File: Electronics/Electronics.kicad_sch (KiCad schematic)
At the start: 0 parts

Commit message: started esp32
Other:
- added sheet Telemetry Module (Telemetry_Module.kicad_sch)
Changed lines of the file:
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@@
 (kicad_sch (version 20230121) (generator eeschema)
   (paper "A4")
+  (sheet (at 132.08 72.39) (size 19.05 19.05) (fields_autoplaced)
+    (stroke (width 0.1524) (type solid))
+    (fill (color 0 0 0 0.0000))
+    (property "Sheetname" "Telemetry Module" (at 132.08 71.6784 0)
+      (effects (font (size 1.27 1.27)) (justify left bottom))
+    )
+    (property "Sheetfile" "Telemetry_Module.kicad_sch" (at 132.08 92.0246 0)
+      (effects (font (size 1.27 1.27)) (justify left top))
+    )
+    (instances
+      (project "Electronics"
+        (path "/4c70cac4-2e87-4919-a1c8-fe5f41acf493" (page "3"))
+      )
+    )
+  )
   (sheet (at 76.2 71.12) (size 21.59 24.13) (fields_autoplaced)
     (stroke (width 0.1524) (type solid))

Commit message: BMI270 schem
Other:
- added sheet Gyroscope (bmi270.kicad_sch)
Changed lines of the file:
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@@
+    )
+  )
+  (sheet (at 138.43 107.95) (size 21.59 20.32) (fields_autoplaced)
+    (stroke (width 0.1524) (type solid))
+    (fill (color 0 0 0 0.0000))
+    (property "Sheetname" "Gyroscope" (at 138.43 107.2384 0)
+      (effects (font (size 1.27 1.27)) (justify left bottom))
+    )
+    (property "Sheetfile" "bmi270.kicad_sch" (at 138.43 128.8546 0)
+      (effects (font (size 1.27 1.27)) (justify left top))
+    )
+    (instances
+      (project "Electronics"
+        (path "/4c70cac4-2e87-4919-a1c8-fe5f41acf493" (page "4"))
+      )
     )
   )

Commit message: rename telemetry
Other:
- sheet Gyroscope renamed Gyro Controller
- sheet Telemetry Module renamed Telemetry and Control Module
- sheet Gyro Controller: file bmi270.kicad_sch -> Gyro_Controller.kicad_sch
- sheet Telemetry and Control Module: file Telemetry_Module.kicad_sch -> Telemetry_And_Control.kicad_sch
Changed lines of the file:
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@@
     (stroke (width 0.1524) (type solid))
     (fill (color 0 0 0 0.0000))
-    (property "Sheetname" "Telemetry Module" (at 132.08 71.6784 0)
+    (property "Sheetname" "Telemetry and Control Module" (at 132.08 71.6784 0)
       (effects (font (size 1.27 1.27)) (justify left bottom))
     )
-    (property "Sheetfile" "Telemetry_Module.kicad_sch" (at 132.08 92.0246 0)
+    (property "Sheetfile" "Telemetry_And_Control.kicad_sch" (at 132.08 92.0246 0)
       (effects (font (size 1.27 1.27)) (justify left top))
     )
@@
     )
   )
-  (sheet (at 138.43 107.95) (size 21.59 20.32) (fields_autoplaced)
+  (sheet (at 76.2 104.14) (size 21.59 20.32) (fields_autoplaced)
     (stroke (width 0.1524) (type solid))
     (fill (color 0 0 0 0.0000))
-    (property "Sheetname" "Gyroscope" (at 138.43 107.2384 0)
+    (property "Sheetname" "Gyro Controller" (at 76.2 103.4284 0)
       (effects (font (size 1.27 1.27)) (justify left bottom))
     )
-    (property "Sheetfile" "bmi270.kicad_sch" (at 138.43 128.8546 0)
+    (property "Sheetfile" "Gyro_Controller.kicad_sch" (at 76.2 125.0446 0)
       (effects (font (size 1.27 1.27)) (justify left top))
     )

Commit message: updates
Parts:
- added BT1: Battery, symbol Device:Battery
- added BT2: 4xAA, symbol Device:Battery
- added C29, C44: 22uF, symbol Device:C_Polarized
- added C43: C, symbol Device:C
- added D6: D, symbol Device:D
- added P1: USB_C_Plug_USB2.0, symbol Connector:USB_C_Plug_USB2.0
- added R18, R19, R21: 1k, symbol Device:R
- added SW5: SW_DIP_x02, symbol Switch:SW_DIP_x02
- added U10: ~, Package_DFN_QFN:QFN-16-1EP_3x3mm_P0.5mm_EP1.7x1.7mm, symbol FSUSB74:FSUSB74
- added U11, U12: AMS1117-3.3, Package_TO_SOT_SMD:SOT-223-3_TabPin2, symbol Regulator_Linear:AMS1117-3.3
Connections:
- new net: BT1.2 (-), U12.1 (GND)
- new net: BT2.1 (+), U12.3 (VI)
- new net: R19.1, SW5.3, U10.6 (SEL0)
- new net: R21.1, U10.15 (/OE)
- new net: R18.1, SW5.4, U10.5 (SEL1)
- new net: D6.1 (K), P1.A4 (VBUS), P1.A9 (VBUS), P1.B4 (VBUS), P1.B9 (VBUS), U11.3 (VI)
- new net: BT1.1 (+), BT2.2 (-)
- new net D+: P1.A6 (D+), U10.2 (D+)
- new net D-: P1.A7 (D-), U10.3 (D-)
- new net GND: C29.2, P1.A1 (GND), P1.A12 (GND), P1.B1 (GND), P1.B12 (GND), P1.S1 (SHIELD), R18.2, R19.2, R21.2, U10.1 (GND), U11.1 (GND)
- new net Gyro Controller/USB+: U10.13 (HSD0+)
- new net Gyro Controller/USB-: U10.14 (HSD0-)
- new net Motor Controller/USB+: U10.11 (HSD1+)
- new net Motor Controller/USB-: U10.12 (HSD1-)
- new net VCC: C29.1, D6.2 (A), SW5.1, SW5.2, U10.4 (VCC), U11.2 (VO)
- no-connect marks 0 -> 4
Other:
- sheet Gyro Controller ports: added READY, SCL, SDA, USB+, USB-; removed none
- sheet Motor Controller ports: added ML_A1, ML_A2, ML_B1, ML_B2, MR_A1, MR_A2, MR_B1, MR_B2, READY, SCL, SDA, USB+, USB-, VBAT; removed none

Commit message: mostly done, needs review, needs pins
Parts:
- added R25, R26: 2.2k, symbol Device:R
- C43: value C -> 100nF
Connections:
- net Gyro Controller/SCL: now also R26.2
- net Gyro Controller/SDA: now also R25.2
- net VCC: now also C43.1, C44.1, U12.2 (VO), R25.1, R26.1
- net at C44.2: now also BT1.2 (-), C43.2, U12.1 (GND)
- net VBAT: now reaches BT2.1 (+), U12.3 (VI)
- net Telemetry and Control Module/USB+: now reaches U10.10 (HSD2+)
- net Telemetry and Control Module/USB-: now reaches U10.9 (HSD2-)
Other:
- sheet Telemetry and Control Module ports: added SCL, SDA, USB+, USB-; removed none
- moved on the sheet: BT1, BT2, C29, C43, C44, D6, P1, R18, R19, R21, SW5, U10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

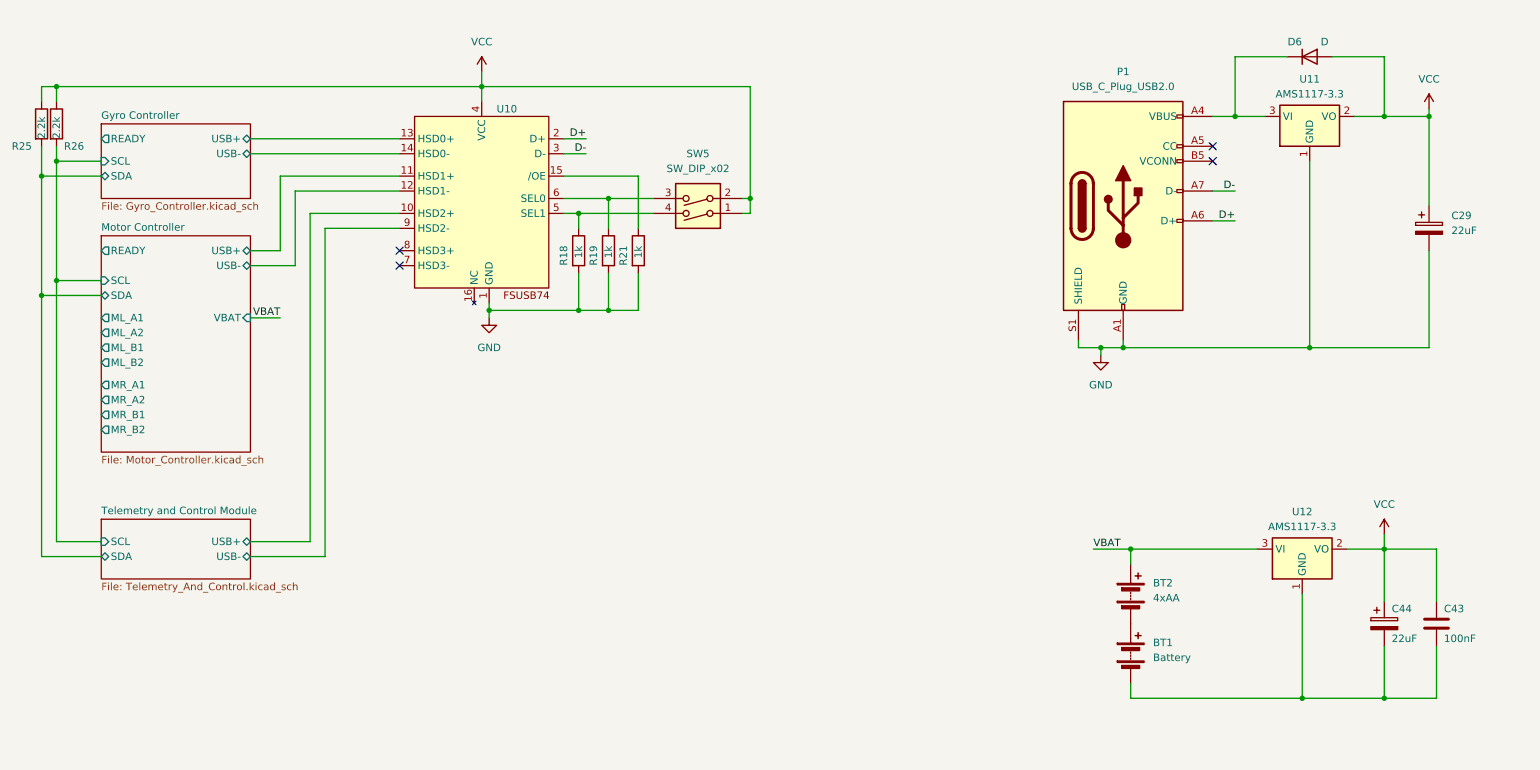
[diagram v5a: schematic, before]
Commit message: oled displays
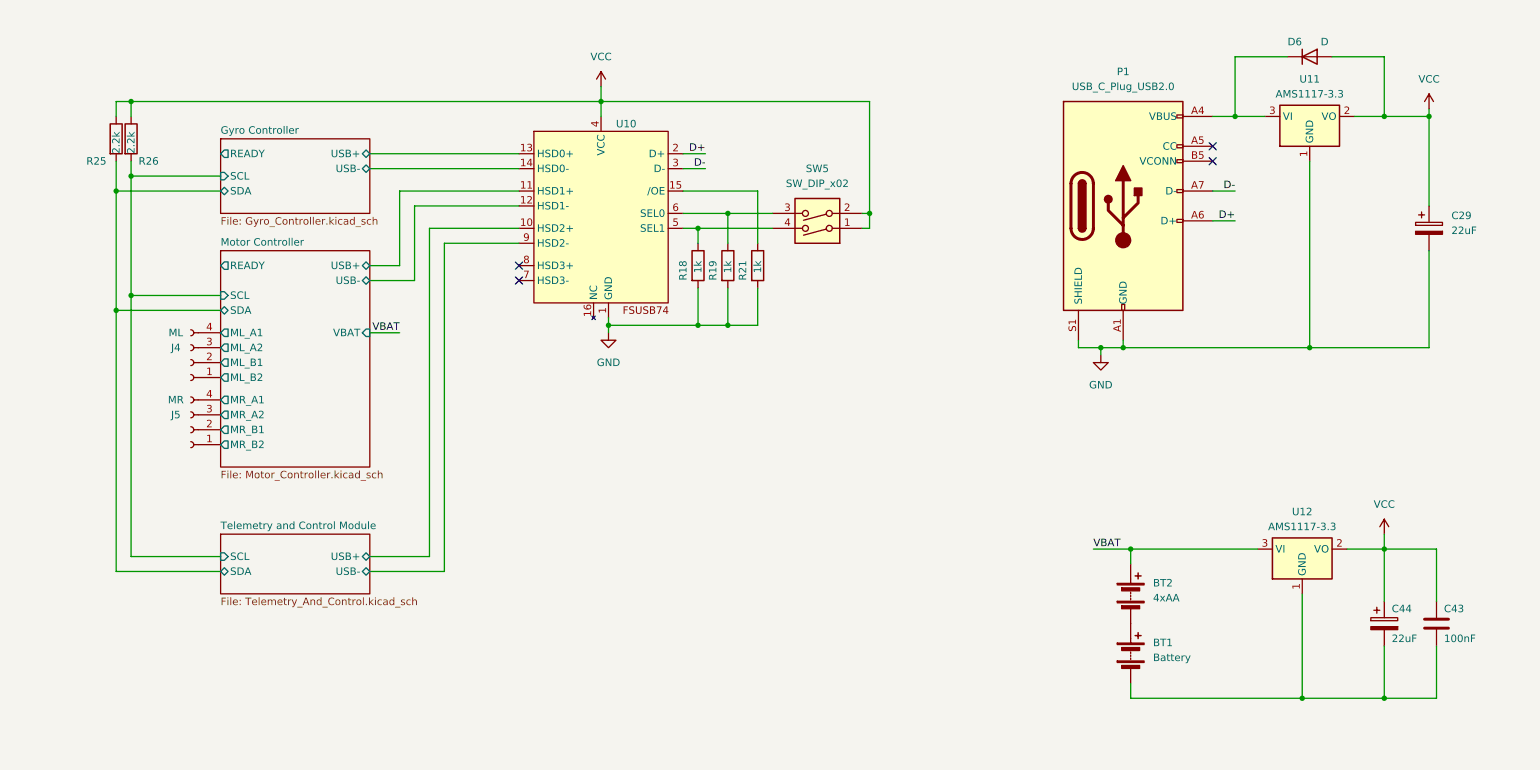
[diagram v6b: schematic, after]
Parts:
- added J4: ML, symbol Connector:Conn_01x04_Socket
- added J5: MR, symbol Connector:Conn_01x04_Socket
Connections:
- net Motor Controller/ML_A1: now also J4.4 (Pin_4)
- net Motor Controller/ML_A2: now also J4.3 (Pin_3)
- net Motor Controller/ML_B1: now also J4.2 (Pin_2)
- net Motor Controller/ML_B2: now also J4.1 (Pin_1)
- net Motor Controller/MR_A1: now also J5.4 (Pin_4)
- net Motor Controller/MR_A2: now also J5.3 (Pin_3)
- net Motor Controller/MR_B1: now also J5.2 (Pin_2)
- net Motor Controller/MR_B2: now also J5.1 (Pin_1)
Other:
- moved on the sheet: R18, R19, R21, R25, R26, SW5, U10

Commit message: buttons
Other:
- sheet Telemetry and Control Module ports: added READY1, READY2; removed none
- moved on the sheet: R25, R26
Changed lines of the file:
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@@
   (junction (at 143.51 52.07) (diameter 0) (color 0 0 0 0)
   )
-  (junction (at 41.91 33.02) (diameter 0) (color 0 0 0 0)
+  (junction (at 34.29 33.02) (diameter 0) (color 0 0 0 0)
   )
   (junction (at 241.3 134.62) (diameter 0) (color 0 0 0 0)
   )
-  (junction (at 41.91 45.72) (diameter 0) (color 0 0 0 0)
+  (junction (at 34.29 45.72) (diameter 0) (color 0 0 0 0)
   )
   (junction (at 262.89 35.56) (diameter 0) (color 0 0 0 0)
@@
   (junction (at 255.27 35.56) (diameter 0) (color 0 0 0 0)
   )
-  (junction (at 39.37 68.58) (diameter 0) (color 0 0 0 0)
+  (junction (at 31.75 68.58) (diameter 0) (color 0 0 0 0)
   )
   (junction (at 229.87 35.56) (diameter 0) (color 0 0 0 0)
@@
   (junction (at 138.43 54.61) (diameter 0) (color 0 0 0 0)
   )
-  (junction (at 39.37 48.26) (diameter 0) (color 0 0 0 0)
-  )
-  (junction (at 41.91 66.04) (diameter 0) (color 0 0 0 0)
+  (junction (at 31.75 48.26) (diameter 0) (color 0 0 0 0)
+  )
+  (junction (at 34.29 66.04) (diameter 0) (color 0 0 0 0)
   )
   (no_connect (at 107.95 60.96))
@@
   (no_connect (at 226.06 40.64))
   (no_connect (at 107.95 63.5))
-  (wire (pts (xy 39.37 113.03) (xy 57.15 113.03))
+  (wire (pts (xy 31.75 113.03) (xy 57.15 113.03))
     (stroke (width 0) (type default))
   )
@@
     (stroke (width 0) (type default))
   )
-  (wire (pts (xy 41.91 33.02) (xy 121.92 33.02))
-    (stroke (width 0) (type default))
-  )
-  (wire (pts (xy 39.37 43.18) (xy 39.37 48.26))
-    (stroke (width 0) (type default))
-  )
-  (wire (pts (xy 41.91 35.56) (xy 41.91 33.02))
+  (wire (pts (xy 34.29 33.02) (xy 121.92 33.02))
+    (stroke (width 0) (type default))
+  )
+  (wire (pts (xy 31.75 43.18) (xy 31.75 48.26))
+    (stroke (width 0) (type default))
+  )
+  (wire (pts (xy 34.29 35.56) (xy 34.29 33.02))
     (stroke (width 0) (type default))
   )
@@
     (stroke (width 0) (type default))
   )
-  (wire (pts (xy 41.91 66.04) (xy 41.91 45.72))
+  (wire (pts (xy 34.29 66.04) (xy 34.29 45.72))
     (stroke (width 0) (type default))
   )
@@
     (stroke (width 0) (type default))
   )
-  (wire (pts (xy 41.91 110.49) (xy 41.91 66.04))
+  (wire (pts (xy 34.29 110.49) (xy 34.29 66.04))
     (stroke (width 0) (type default))
   )
@@
     (stroke (width 0) (type default))
   )
+  (wire (pts (xy 43.18 41.91) (xy 57.15 41.91))
+    (stroke (width 0) (type default))
+  )
   (wire (pts (xy 138.43 54.61) (xy 151.13 54.61))
     (stroke (width 0) (type default))
   )
-  (wire (pts (xy 57.15 66.04) (xy 41.91 66.04))
+  (wire (pts (xy 57.15 66.04) (xy 34.29 66.04))
     (stroke (width 0) (type default))
   )
@@
     (stroke (width 0) (type default))
   )
-  (wire (pts (xy 57.15 48.26) (xy 39.37 48.26))
+  (wire (pts (xy 57.15 48.26) (xy 31.75 48.26))
     (stroke (width 0) (type default))
   )
@@
     (stroke (width 0) (type default))
   )
-  (wire (pts (xy 39.37 33.02) (xy 41.91 33.02))
-    (stroke (width 0) (type default))
-  )
-  (wire (pts (xy 39.37 48.26) (xy 39.37 68.58))
+  (wire (pts (xy 31.75 33.02) (xy 34.29 33.02))
+    (stroke (width 0) (type default))
+  )
+  (wire (pts (xy 31.75 48.26) (xy 31.75 68.58))
     (stroke (width 0) (type default))
   )
@@
     (stroke (width 0) (type default))
   )
+  (wire (pts (xy 57.15 119.38) (xy 43.18 119.38))
+    (stroke (width 0) (type default))
+  )
   (wire (pts (xy 238.76 25.4) (xy 229.87 25.4))
     (stroke (width 0) (type default))
@@
     (stroke (width 0) (type default))
   )
-  (wire (pts (xy 39.37 68.58) (xy 57.15 68.58))
+  (wire (pts (xy 45.72 116.84) (xy 45.72 60.96))
+    (stroke (width 0) (type default))
+  )
+  (wire (pts (xy 31.75 68.58) (xy 57.15 68.58))
     (stroke (width 0) (type default))
   )
@@
     (stroke (width 0) (type default))
   )
-  (wire (pts (xy 39.37 68.58) (xy 39.37 113.03))
+  (wire (pts (xy 31.75 68.58) (xy 31.75 113.03))
     (stroke (width 0) (type default))
   )
@@
     (stroke (width 0) (type default))
   )
+  (wire (pts (xy 57.15 116.84) (xy 45.72 116.84))
+    (stroke (width 0) (type default))
+  )
   (wire (pts (xy 135.89 41.91) (xy 139.7 41.91))
     (stroke (width 0) (type default))
   )
-  (wire (pts (xy 39.37 33.02) (xy 39.37 35.56))
+  (wire (pts (xy 31.75 33.02) (xy 31.75 35.56))
     (stroke (width 0) (type default))
   )
@@
     (stroke (width 0) (type default))
   )
-  (wire (pts (xy 41.91 45.72) (xy 57.15 45.72))
+  (wire (pts (xy 43.18 119.38) (xy 43.18 41.91))
+    (stroke (width 0) (type default))
+  )
+  (wire (pts (xy 34.29 45.72) (xy 57.15 45.72))
     (stroke (width 0) (type default))
   )
@@
     (stroke (width 0) (type default))
   )
-  (wire (pts (xy 57.15 110.49) (xy 41.91 110.49))
+  (wire (pts (xy 57.15 110.49) (xy 34.29 110.49))
     (stroke (width 0) (type default))
   )
@@
     (stroke (width 0) (type default))
   )
-  (wire (pts (xy 41.91 43.18) (xy 41.91 45.72))
+  (wire (pts (xy 34.29 43.18) (xy 34.29 45.72))
     (stroke (width 0) (type default))
   )
@@
   )
   (wire (pts (xy 229.87 35.56) (xy 234.95 35.56))
+    (stroke (width 0) (type default))
+  )
+  (wire (pts (xy 45.72 60.96) (xy 57.15 60.96))
     (stroke (width 0) (type default))
   )
@@
     )
   )
-  (symbol (lib_id "Device:R") (at 41.91 39.37 0) (unit 1)
-    (in_bom yes) (on_board yes) (dnp no)
-    (property "Reference" "R26" (at 43.18 43.18 0)
-      (effects (font (size 1.27 1.27)) (justify left))
-    )
-    (property "Value" "2.2k" (at 41.91 41.91 90)
-      (effects (font (size 1.27 1.27)) (justify left))
-    )
-    (property "Footprint" "" (at 40.132 39.37 90)
-      (effects (font (size 1.27 1.27)) hide)
-    )
-    (property "Datasheet" "~" (at 41.91 39.37 0)
+  (symbol (lib_id "Device:R") (at 34.29 39.37 0) (unit 1)
+    (in_bom yes) (on_board yes) (dnp no)
+    (property "Reference" "R26" (at 35.56 43.18 0)
+      (effects (font (size 1.27 1.27)) (justify left))
+    )
+    (property "Value" "2.2k" (at 34.29 41.91 90)
+      (effects (font (size 1.27 1.27)) (justify left))
+    )
+    (property "Footprint" "" (at 32.512 39.37 90)
+      (effects (font (size 1.27 1.27)) hide)
+    )
+    (property "Datasheet" "~" (at 34.29 39.37 0)
       (effects (font (size 1.27 1.27)) hide)
     )
@@
     )
   )
-  (symbol (lib_id "Device:R") (at 39.37 39.37 0) (unit 1)
-    (in_bom yes) (on_board yes) (dnp no)
-    (property "Reference" "R25" (at 34.29 43.18 0)
-      (effects (font (size 1.27 1.27)) (justify left))
-    )
-    (property "Value" "2.2k" (at 39.37 41.91 90)
-      (effects (font (size 1.27 1.27)) (justify left))
-    )
-    (property "Footprint" "" (at 37.592 39.37 90)
-      (effects (font (size 1.27 1.27)) hide)
-    )
-    (property "Datasheet" "~" (at 39.37 39.37 0)
+  (symbol (lib_id "Device:R") (at 31.75 39.37 0) (unit 1)
+    (in_bom yes) (on_board yes) (dnp no)
+    (property "Reference" "R25" (at 26.67 43.18 0)
+      (effects (font (size 1.27 1.27)) (justify left))
+    )
+    (property "Value" "2.2k" (at 31.75 41.91 90)
+      (effects (font (size 1.27 1.27)) (justify left))
+    )
+    (property "Footprint" "" (at 29.972 39.37 90)
+      (effects (font (size 1.27 1.27)) hide)
+    )
+    (property "Datasheet" "~" (at 31.75 39.37 0)
       (effects (font (size 1.27 1.27)) hide)
     )
@@
     )
   )
-  (sheet (at 57.15 106.68) (size 25.4 10.16) (fields_autoplaced)
+  (sheet (at 57.15 106.68) (size 25.4 17.78) (fields_autoplaced)
     (stroke (width 0.1524) (type solid))
     (fill (color 255 255 194 1.0000))
@@
       (effects (font (size 1.27 1.27)) (justify left bottom))
     )
-    (property "Sheetfile" "Telemetry_And_Control.kicad_sch" (at 57.15 117.4246 0)
+    (property "Sheetfile" "Telemetry_And_Control.kicad_sch" (at 57.15 125.0446 0)
       (effects (font (size 1.27 1.27)) (justify left top))
     )
@@
       (effects (font (size 1.27 1.27)) (justify left))
     )
+    (pin "READY1" input (at 57.15 116.84 180)
+      (effects (font (size 1.27 1.27)) (justify left))
+    )
+    (pin "READY2" input (at 57.15 119.38 180)
+      (effects (font (size 1.27 1.27)) (justify left))
+    )

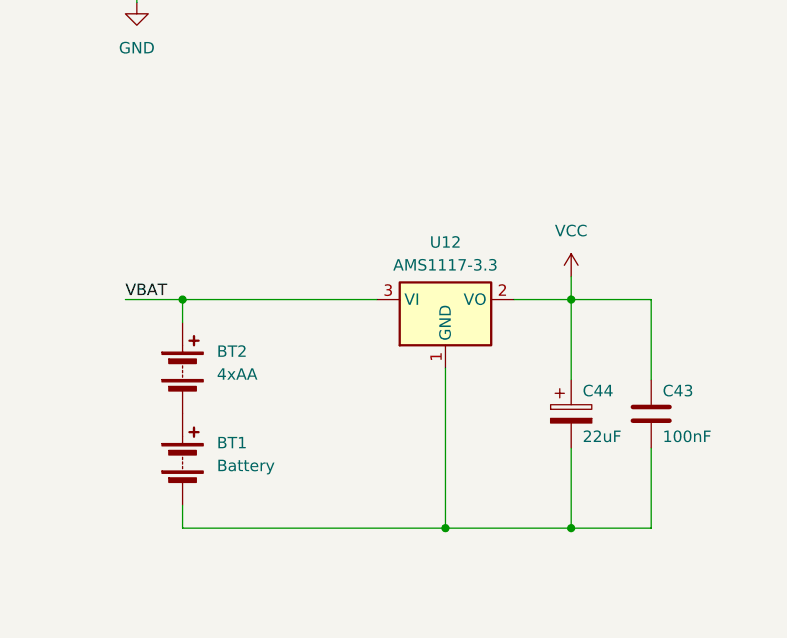
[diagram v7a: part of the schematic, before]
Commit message: started pcb, need bigger frame
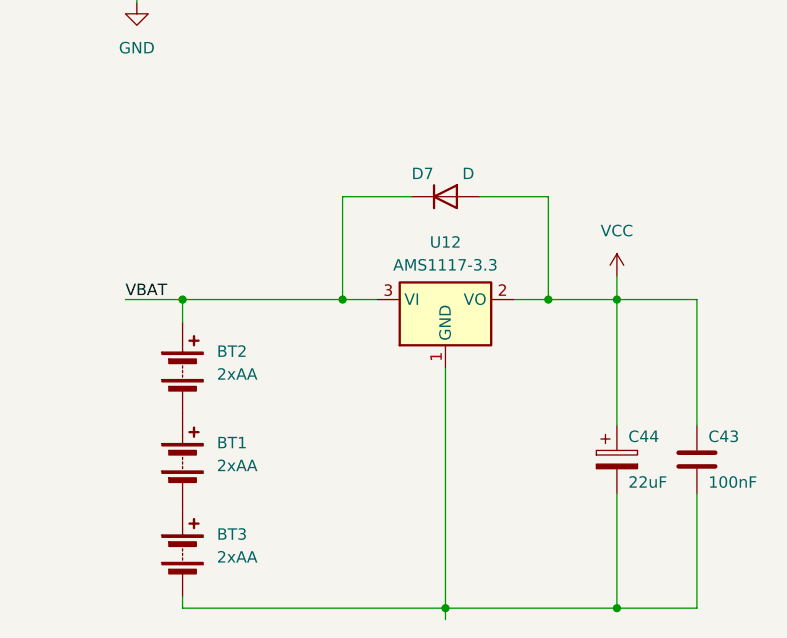
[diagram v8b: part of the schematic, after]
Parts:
- added BT3: 2xAA, Battery:BatteryHolder_Keystone_2462_2xAA, symbol Device:Battery
- added D7: D, Resistor_SMD:R_0201_0603Metric, symbol Device:D
- BT1: value Battery -> 2xAA; footprint (none) -> Battery:BatteryHolder_Keystone_2479_3xAAA
- BT2: value 4xAA -> 2xAA; footprint (none) -> Battery:BatteryHolder_Keystone_2462_2xAA
- C29, C44: footprint (none) -> Capacitor_SMD:CP_Elec_6.3x5.9
- C43: footprint (none) -> Capacitor_SMD:C_0201_0603Metric
- D6, R18, R19, R21, R25, R26: footprint (none) -> Resistor_SMD:R_0201_0603Metric
- J4, J5: footprint (none) -> Connector_JST:JST_PH_B4B-PH-K_1x04_P2.00mm_Vertical
- P1: footprint (none) -> Connector_USB:USB_C_Receptacle_Molex_105450-0101
- SW5: footprint (none) -> Button_Switch_SMD:SW_SPST_TL3342
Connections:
- net VBAT: now also D7.1 (K)
- net VCC: now also D7.2 (A)
- net at C43.2, C44.2, U12.1 (GND): now also BT3.2 (-); no longer BT1.2 (-)
- new net: BT1.2 (-), BT3.1 (+)
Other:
- moved on the sheet: C43, C44
